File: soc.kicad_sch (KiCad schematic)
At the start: 64 parts, among them U1 MPFS250T-FCVG484

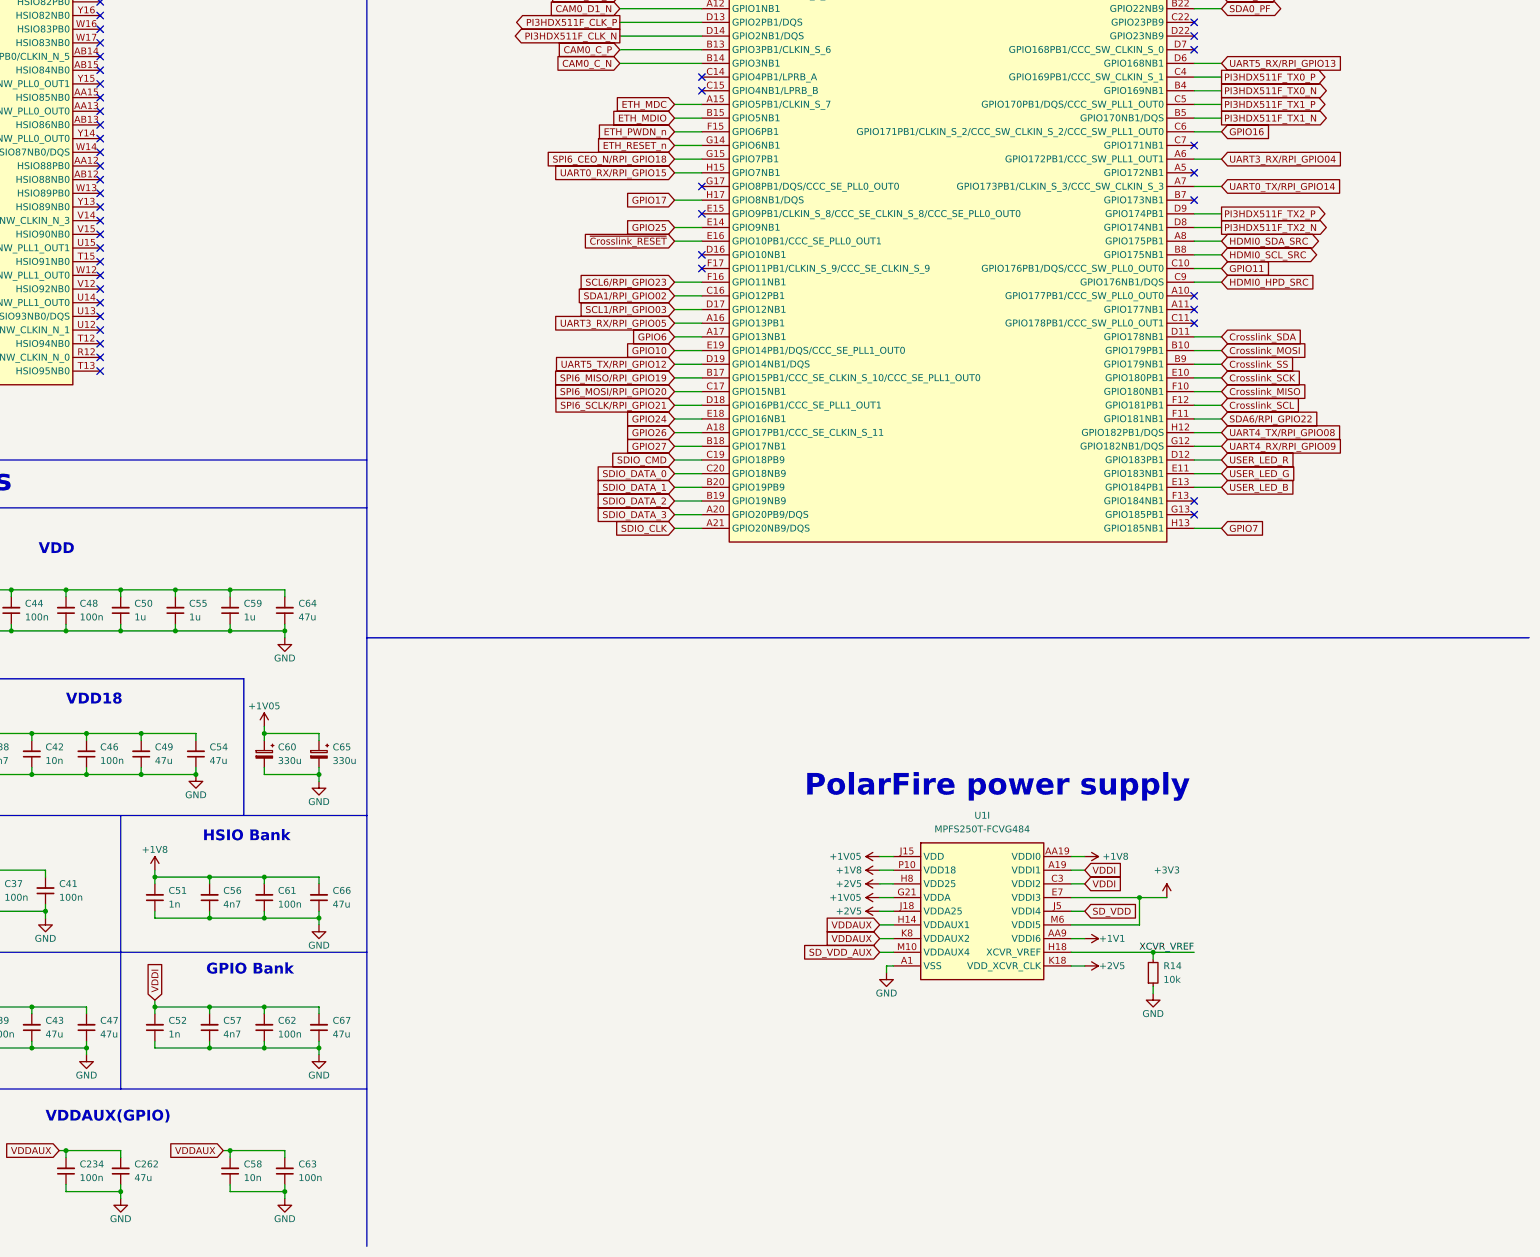
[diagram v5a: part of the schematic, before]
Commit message: [#57038] Add clock sources and logic shifters, change ETH PHY supply
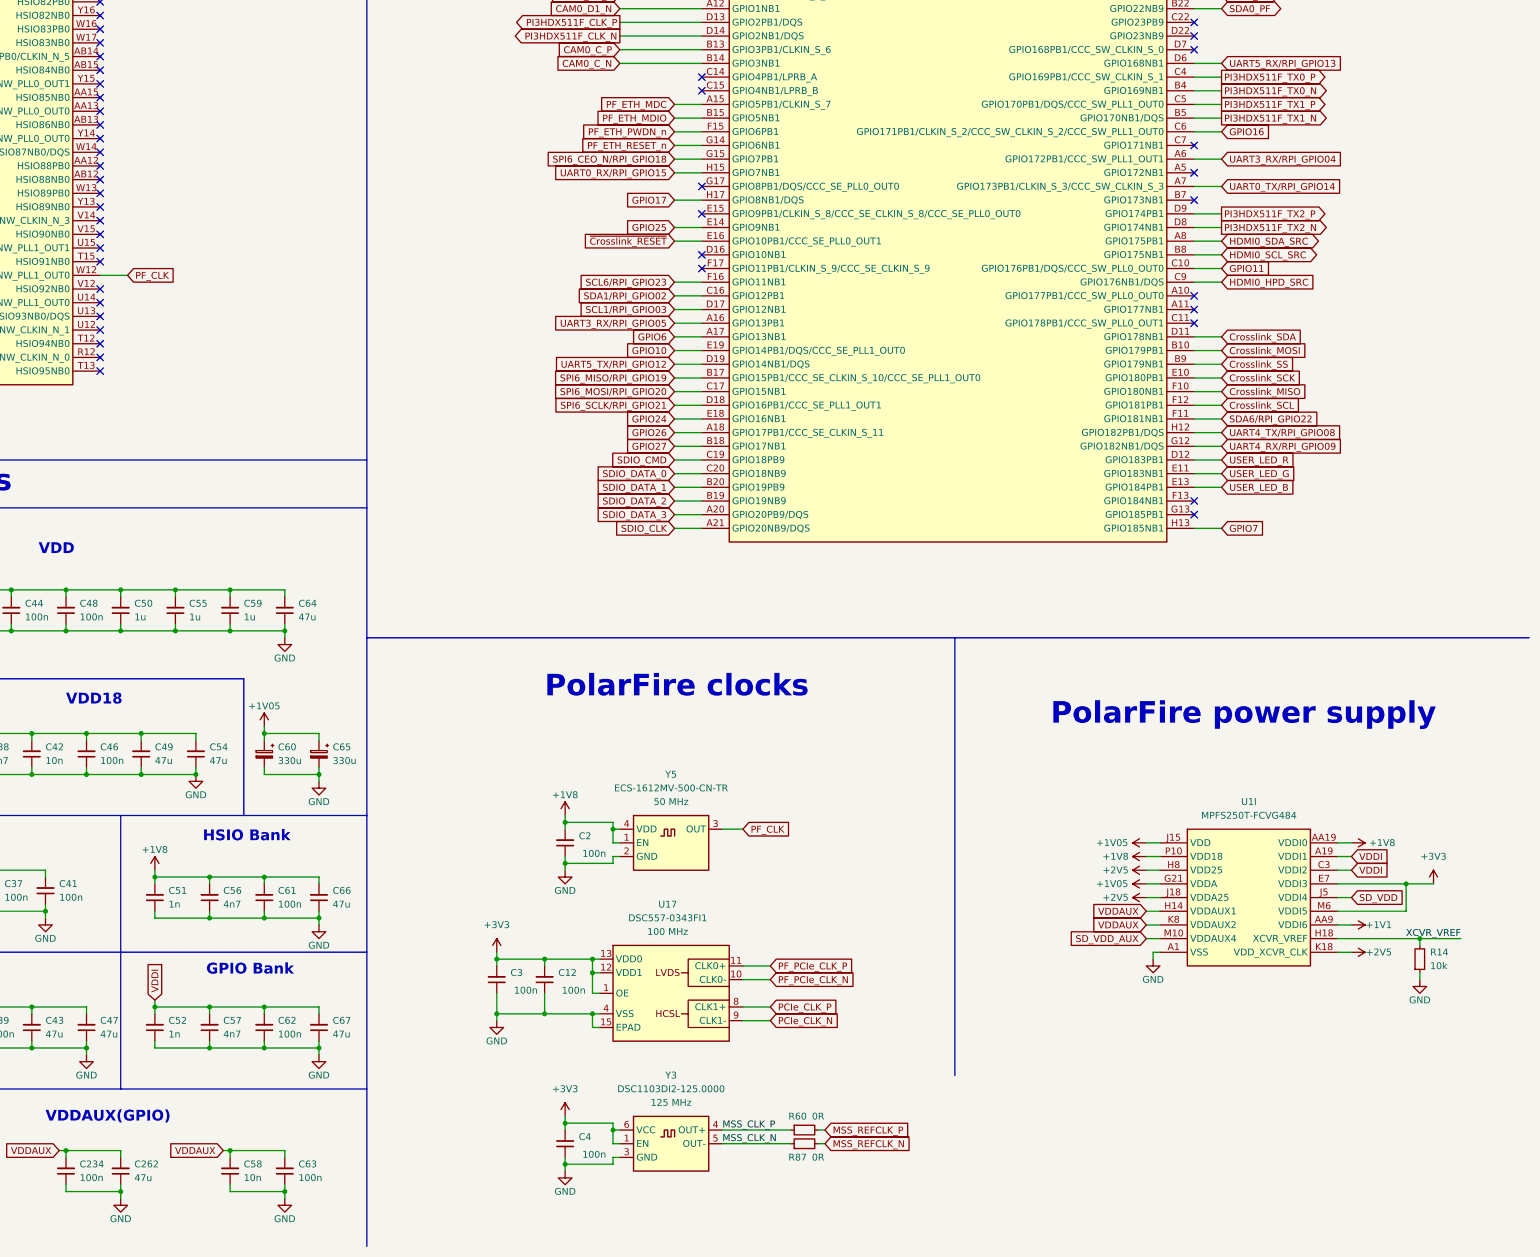
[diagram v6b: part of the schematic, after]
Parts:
- added C12, C2, C3, C4: C_100n_0402, antmicro-footprints:C_0402_1005Metric, symbol antmicroCapacitors0402:C_100n_0402
- added R60, R87: R_0R_0402, antmicro-footprints:R_0402_1005Metric, symbol antmicroResistors0402:R_0R_0402
- added U17: DSC557-0343FI1, antmicro-footprints:VQFN-14-1EP_3.2x2.5mm_P0.5mm_Layout4x3, symbol antmicroClockTimingRealTimeClocks:DSC557-0343FI1
- added Y3: Oscillator_125MHz_DSC1103DI2, antmicro-footprints:Oscillator_SMD_Microchip_DSC1103DI2_2.5x2x0.85mm, symbol antmicroOscillators:Oscillator_125MHz_DSC1103DI2
- added Y5: Oscillator_50MHz_ECS_1612MV, antmicro-footprints:Oscillator_SMD_ECS_1612MV_1.6x1.2x0.6mm, symbol antmicroOscillators:Oscillator_50MHz_ECS_1612MV
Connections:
- net +1V8: now also C2.2, Y5.1 (EN), Y5.4 (VDD)
- net +3V3: now also C12.2, C3.2, C4.2, U17.1 (OE), U17.12 (VDD1), U17.13 (VDD0), Y3.1 (EN), Y3.6 (VCC)
- net GND: now also C12.1, C2.1, C3.1, C4.1, U17.15 (EPAD), U17.4 (VSS), Y3.3 (GND), Y5.2 (GND)
- net PF_CLK: now reaches U1.W12 (HSIO92PB0/CLKIN_N_2/CCC_NW_CLKIN_N_2/CCC_NW_PLL1_OUT0)
- net PF_CLK: now also Y5.3 (OUT)
- net ETH_MDC renamed PF_ETH_MDC
- net ETH_MDIO renamed PF_ETH_MDIO
- net ETH_PWDN_n renamed PF_ETH_PWDN_n
- net ETH_RESET_n renamed PF_ETH_RESET_n
- new net: U17.14 (NC), U17.2 (NC), U17.3 (NC), U17.5 (NC), U17.6 (NC), U17.7 (NC)
- new net MSS_CLK_N: R87.1, Y3.5 (OUT-)
- new net MSS_CLK_P: R60.1, Y3.4 (OUT+)
- new net MSS_REFCLK_N: R87.2
- new net MSS_REFCLK_P: R60.2
- new net PCIe_CLK_N: U17.9 (CLK1-)
- new net PCIe_CLK_P: U17.8 (CLK1+)
- new net PF_PCIe_CLK_N: U17.10 (CLK0-)
- new net PF_PCIe_CLK_P: U17.11 (CLK0+)
- no-connect marks 51 -> 50
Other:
- note added: "PolarFire clocks"
- moved on the sheet: R14, U1I

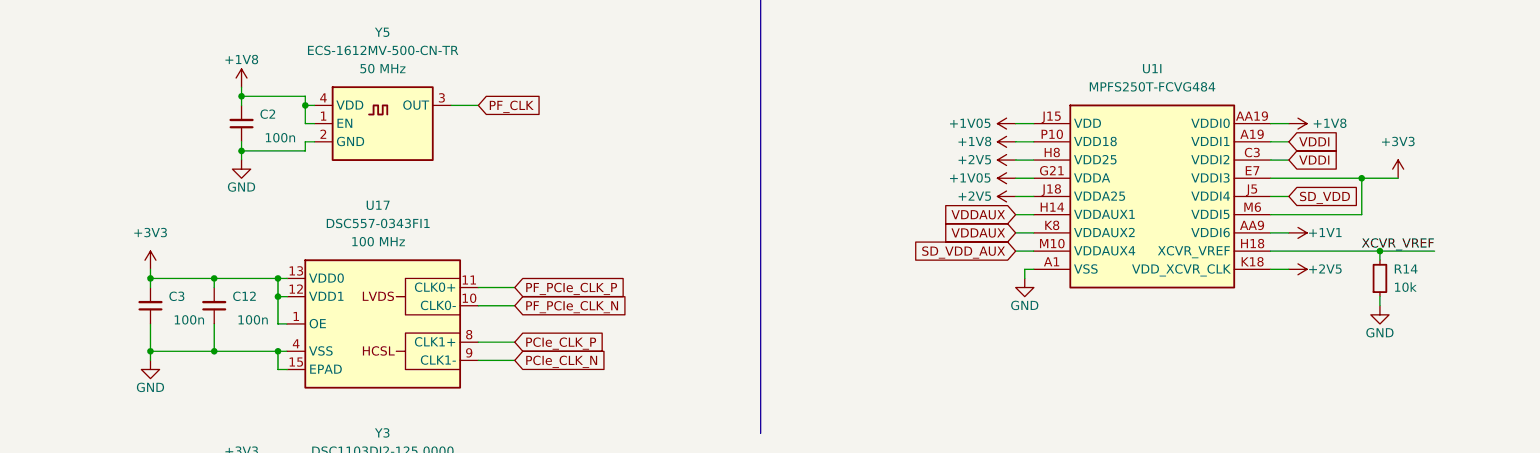
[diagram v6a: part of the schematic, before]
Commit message: [#56952] Place top designators, clean ERC
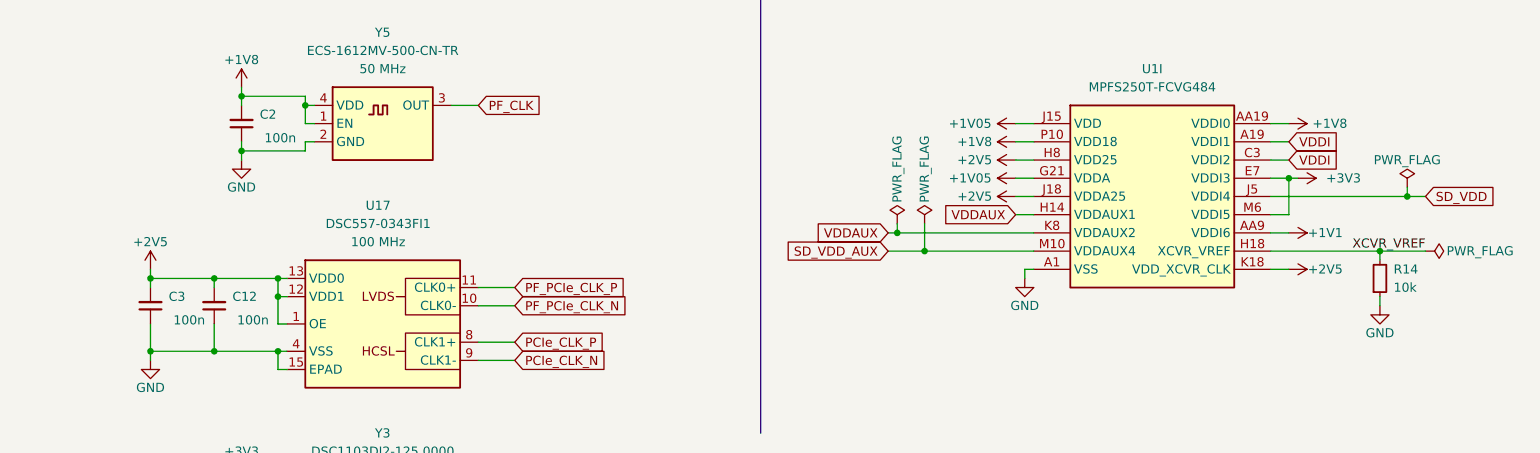
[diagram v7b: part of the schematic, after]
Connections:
- net +2V5: now also C12.2, C3.2, U17.1 (OE), U17.12 (VDD1), U17.13 (VDD0)
- net +3V3: no longer C12.2, C3.2, U17.1 (OE), U17.12 (VDD1), U17.13 (VDD0)

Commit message: Update components
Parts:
- C60, C65: Val 330u/6.3V -> 330u
- Y3: Manufacturer Microchip -> Microchip Technology
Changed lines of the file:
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@@
       (effects (font (size 1.27 1.27) (thickness 0.15)) (justify left bottom) hide)
     )
-    (property "Val" "330u/6.3V" (at 175.26 194.31 90)
+    (property "Val" "330u" (at 175.26 194.31 90)
       (effects (font (size 1.27 1.27) (thickness 0.15)) (justify left) hide)
     )
@@
       (effects (font (size 1.27 1.27) (thickness 0.15)) (justify left bottom) hide)
     )
-    (property "Manufacturer" "Microchip" (at 267.335 267.335 0)
+    (property "Manufacturer" "Microchip Technology" (at 267.335 267.335 0)
       (effects (font (size 1.27 1.27) (thickness 0.15)) (justify left bottom) hide)
     )
@@
       (effects (font (size 1.27 1.27) (thickness 0.15)) (justify left bottom) hide)
     )
-    (property "Val" "330u/6.3V" (at 185.42 194.31 90)
+    (property "Val" "330u" (at 185.42 194.31 90)
       (effects (font (size 1.27 1.27) (thickness 0.15)) (justify left) hide)
     )
